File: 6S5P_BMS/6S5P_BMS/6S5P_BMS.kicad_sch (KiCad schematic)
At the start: 1 part, among them U1 PBQ41Z90PVPT

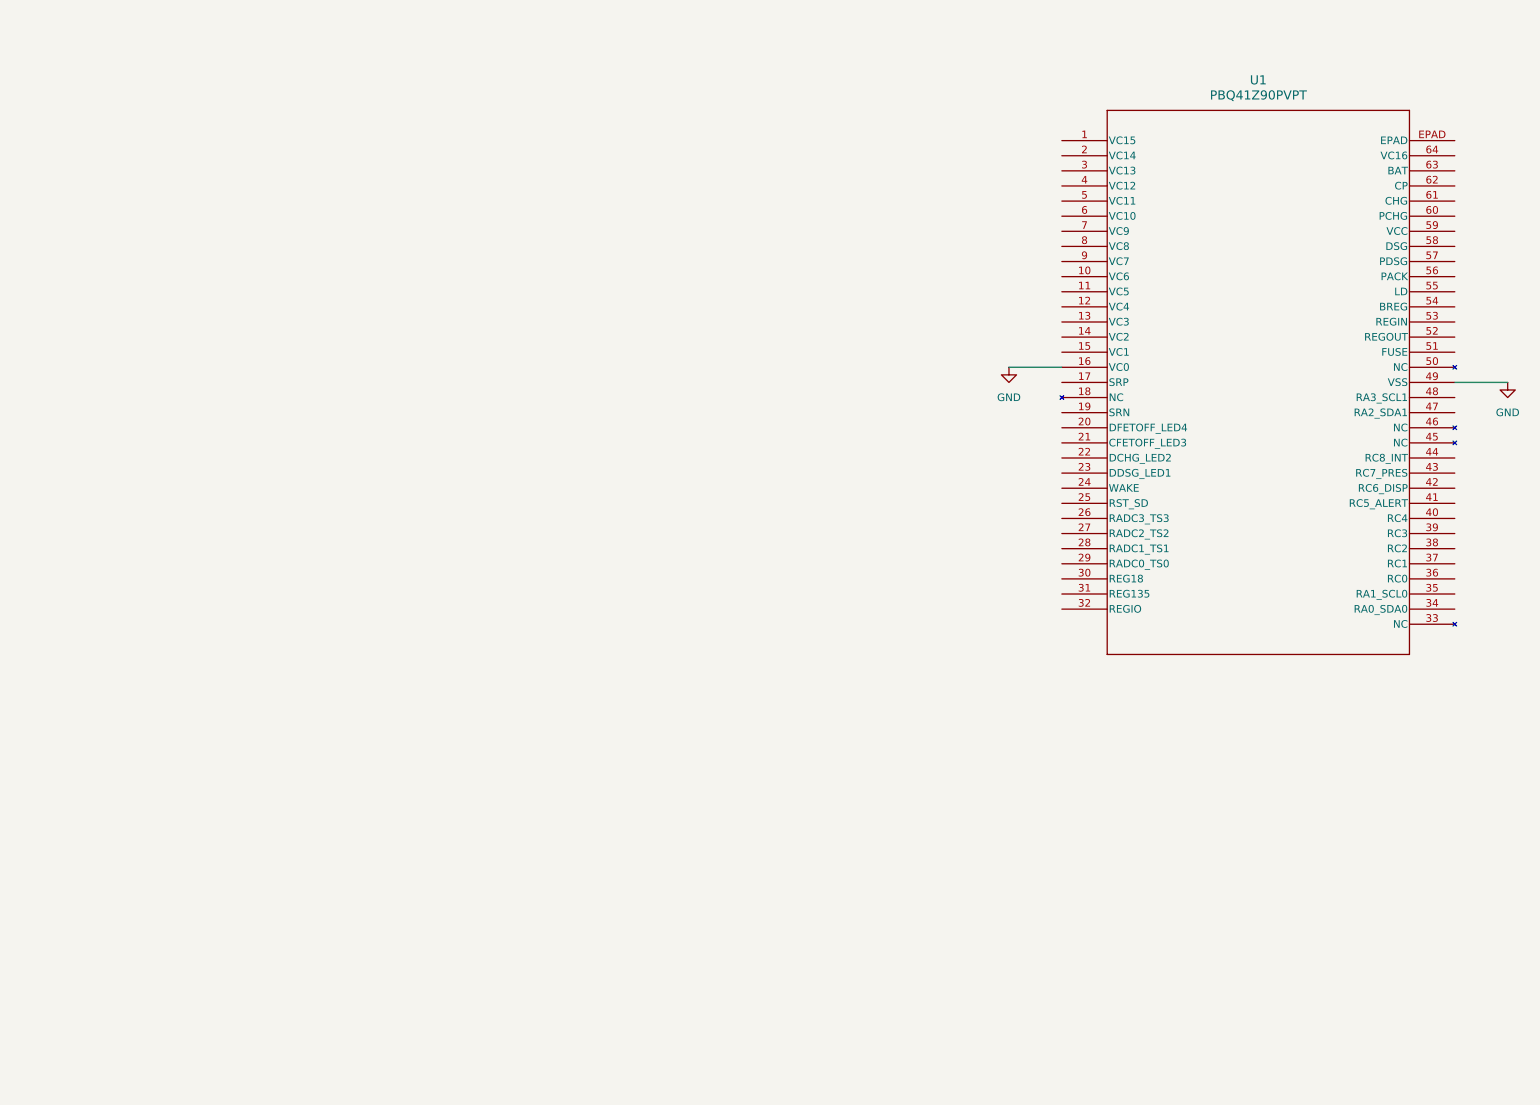
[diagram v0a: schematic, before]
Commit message: Re-upload: external balancing circuit to enable larger balancing current
Balancing current is chosen to be ~250mA. (original max of 100mA)
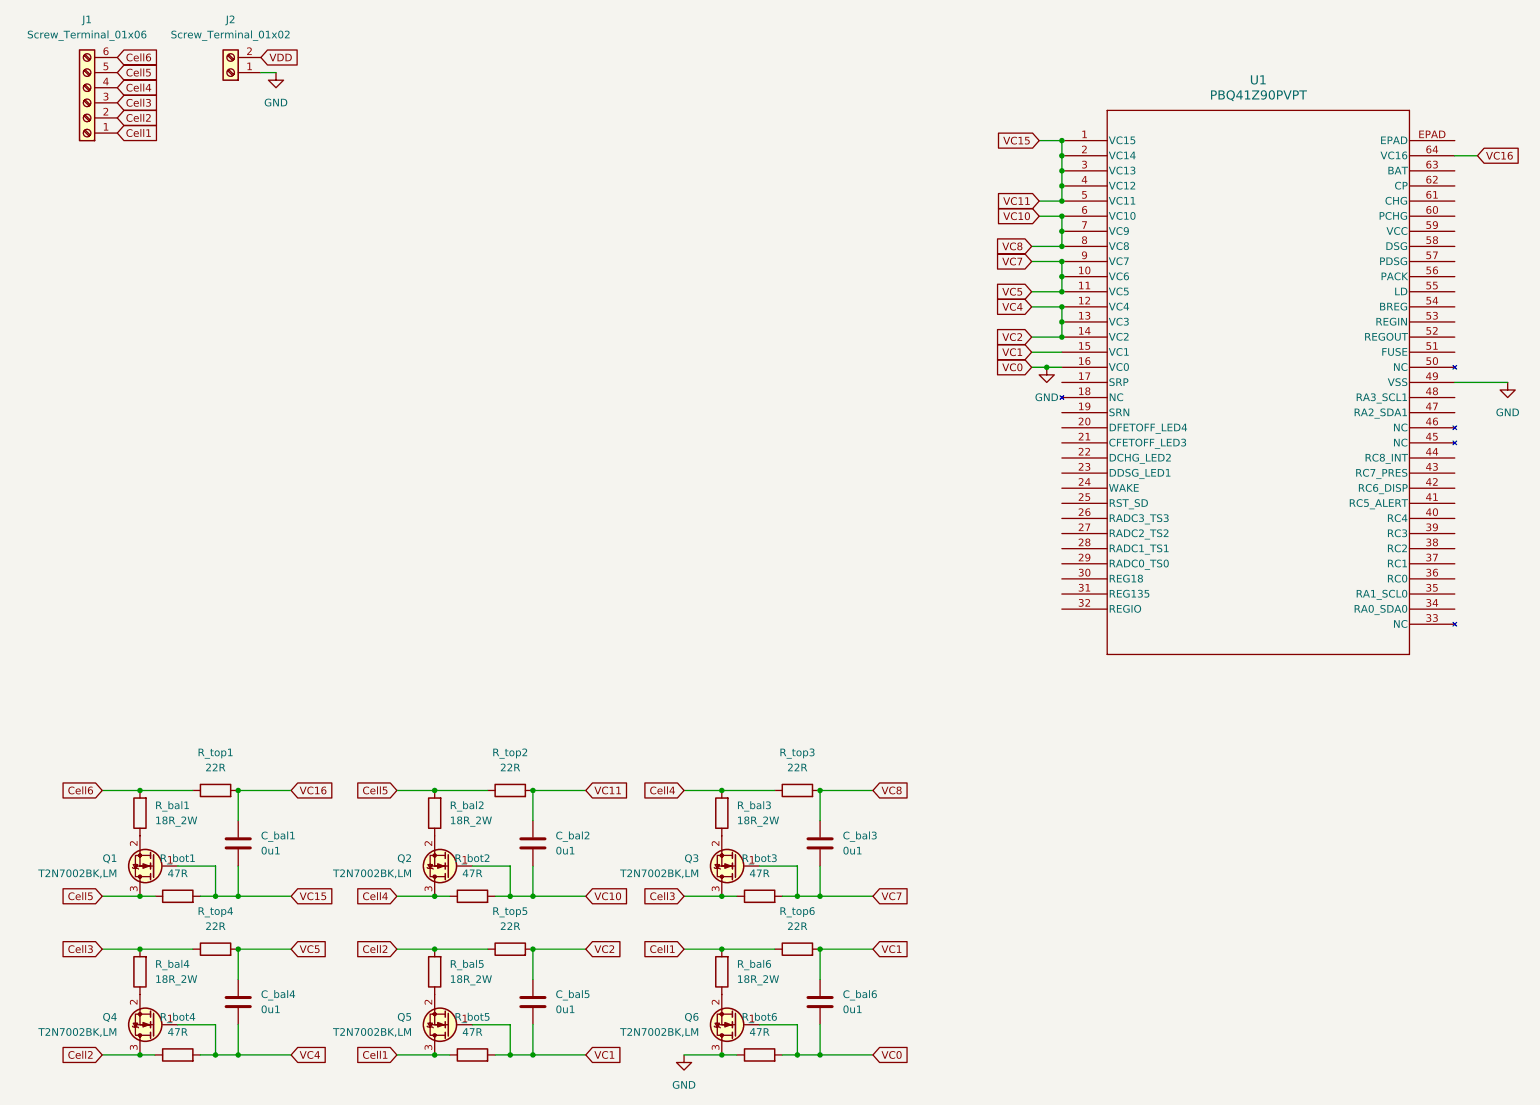
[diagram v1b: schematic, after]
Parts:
- added C_bal1, C_bal2, C_bal3, C_bal4, C_bal5, C_bal6: 0u1, rsx_capacitors:C_0603_1608Metric, symbol rsx_Capacitors:0u1
- added J1: Screw_Terminal_01x06, symbol Connector:Screw_Terminal_01x06
- added J2: Screw_Terminal_01x02, symbol Connector:Screw_Terminal_01x02
- added Q1, Q2, Q3, Q4, Q5, Q6: T2N7002BK,LM, Package_TO_SOT_SMD:SOT-23_Handsoldering, symbol rsx_Transistors:T2N7002BK,LM
- added R_bal1, R_bal2, R_bal3, R_bal4, R_bal5, R_bal6: 18R_2W, rsx_resistors:R_Axial_DIN0516_L15.5mm_D5.0mm_P20.32mm_Horizontal, symbol rsx_Resistors:18R_2W
- added R_bot1, R_bot2, R_bot3, R_bot4, R_bot5, R_bot6: 47R, rsx_resistors:R_0805_2012Metric, symbol rsx_Resistors:47R
- added R_top1, R_top2, R_top3, R_top4, R_top5, R_top6: 22R, rsx_resistors:R_0603_1608Metric, symbol rsx_Resistors:22R
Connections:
- net GND: now also C_bal6.2, J2.1 (Pin_1), Q6.1 (G), Q6.3 (D), R_bot6.1, R_bot6.2
- net VC11: now reaches U1.1 (VC15)
- net VC11: now also U1.2 (VC14), U1.3 (VC13), U1.4 (VC12), U1.5 (VC11), C_bal1.2, C_bal2.1, Q1.1 (G), R_bot1.2, R_top2.2
- net VC5: now reaches U1.10 (VC6)
- net VC5: now also U1.11 (VC5), U1.9 (VC7), C_bal3.2, C_bal4.1, Q3.1 (G), R_bot3.2, R_top4.2
- net VC2: now reaches U1.12 (VC4)
- net VC2: now also U1.13 (VC3), U1.14 (VC2), C_bal4.2, C_bal5.1, Q4.1 (G), R_bot4.2, R_top5.2
- net VC1: now reaches U1.15 (VC1)
- net VC1: now also C_bal5.2, C_bal6.1, Q5.1 (G), R_bot5.2, R_top6.2
- net VC10: now reaches U1.6 (VC10)
- net VC10: now also U1.7 (VC9), U1.8 (VC8), C_bal2.2, C_bal3.1, Q2.1 (G), R_bot2.2, R_top3.2
- net VC16: now reaches U1.64 (VC16)
- net VC16: now also C_bal1.1, R_top1.2
- new net: Q5.2 (S), R_bal5.1
- new net: Q1.2 (S), R_bal1.1
- new net: Q2.2 (S), R_bal2.1
- new net: Q3.2 (S), R_bal3.1
- new net: Q4.2 (S), R_bal4.1
- new net: Q6.2 (S), R_bal6.1
- new net Cell1: J1.1 (Pin_1), Q5.3 (D), R_bal6.2, R_bot5.1, R_top6.1
- new net Cell2: J1.2 (Pin_2), Q4.3 (D), R_bal5.2, R_bot4.1, R_top5.1
- new net Cell3: J1.3 (Pin_3), Q3.3 (D), R_bal4.2, R_bot3.1, R_top4.1
- new net Cell4: J1.4 (Pin_4), Q2.3 (D), R_bal3.2, R_bot2.1, R_top3.1
- new net Cell5: J1.5 (Pin_5), Q1.3 (D), R_bal2.2, R_bot1.1, R_top2.1
- new net Cell6: J1.6 (Pin_6), R_bal1.2, R_top1.1
- new net VDD: J2.2 (Pin_2)

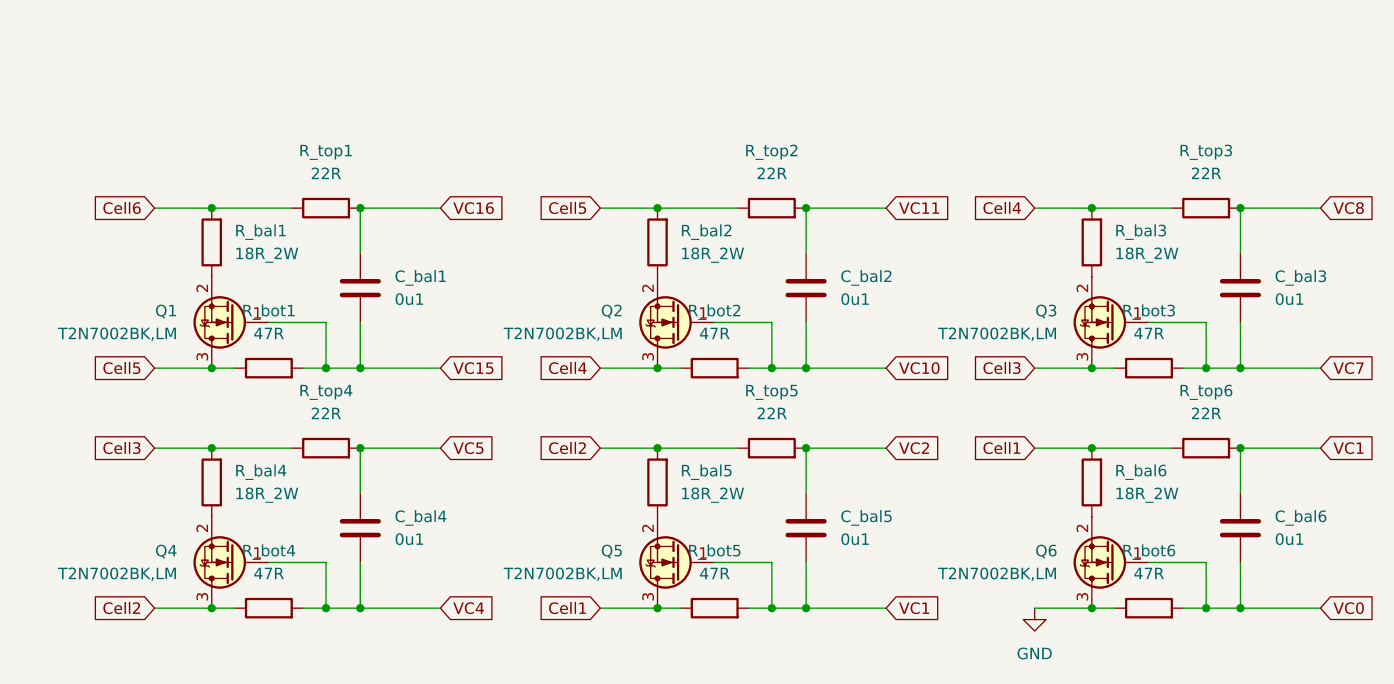
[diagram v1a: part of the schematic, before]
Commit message: Redesigned the external balancing circuit (hopefully last time) to ensure resistances fall between 20 and 100 ohms
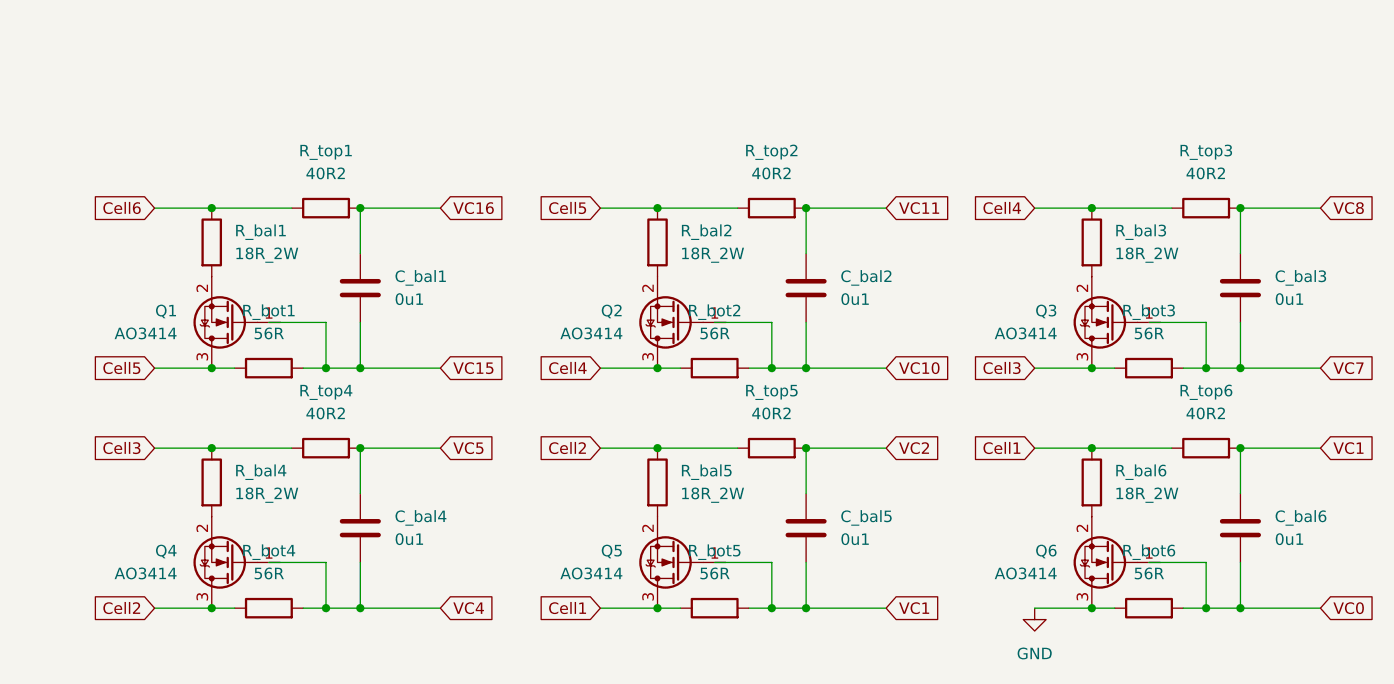
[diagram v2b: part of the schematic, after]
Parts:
- Q1, Q2, Q3, Q4, Q5, Q6: value T2N7002BK,LM -> AO3414; footprint Package_TO_SOT_SMD:SOT-23_Handsoldering -> Package_TO_SOT_SMD:SOT-23; symbol rsx_Transistors:T2N7002BK,LM -> rsx_Transistors:AO3414; DPN T2N7002BKLMCT-ND -> 785-1009-1-ND; Description 1 (none) -> 1=G 2=S 3=D; MPN T2N7002BK,LM -> AO3414; Manufacturer (none) -> Alpha & Omega Semiconductor Inc.
- R_bot1, R_bot2, R_bot3, R_bot4, R_bot5, R_bot6: value 47R -> 56R; footprint rsx_resistors:R_0805_2012Metric -> rsx_resistors:R_0603_1608Metric; symbol rsx_Resistors:47R -> rsx_Resistors:56R; DPN RMCF0805JT47R0CT-ND -> RMCF0603FT56R0CT-ND; MPN RMCF0805JT47R0 -> RMCF0603FT56R0
- R_top1, R_top2, R_top3, R_top4, R_top5, R_top6: value 22R -> 40R2; symbol rsx_Resistors:22R -> rsx_Resistors:40R2; DPN RMCF0603FT22R0CT-ND -> P40.2HCT-ND; MFR Stackpole Electronics Inc -> Panasonic Industry; MPN RMCF0603FT22R0 -> ERJ-3EKF40R2V
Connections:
- net Cell1: now also R_bal6.1; no longer R_bal6.2
- net Cell2: now also R_bal5.1; no longer R_bal5.2
- net Cell3: now also R_bal4.1; no longer R_bal4.2
- net Cell4: now also R_bal3.1; no longer R_bal3.2
- net Cell5: now also R_bal2.1; no longer R_bal2.2
- net Cell6: now also R_bal1.1; no longer R_bal1.2
- net GND: no longer Q6.1 (G)
- net VC1: no longer Q5.1 (G)
- net VC10: no longer Q2.1 (G)
- net VC11: no longer Q1.1 (G)
- net VC2: no longer Q4.1 (G)
- net VC5: no longer Q3.1 (G)
- net at Q5.2 (S): now also R_bal5.2; no longer R_bal5.1
- net at Q1.2 (S): now also R_bal1.2; no longer R_bal1.1
- net at Q2.2 (S): now also R_bal2.2; no longer R_bal2.1
- net at Q3.2 (S): now also R_bal3.2; no longer R_bal3.1
- net at Q4.2 (S): now also R_bal4.2; no longer R_bal4.1
- net at Q6.2 (S): now also R_bal6.2; no longer R_bal6.1
